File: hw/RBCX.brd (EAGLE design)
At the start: 100 x 100 mm, 463 parts, among them IC1 AMS1117-3.3, IC10 INA180A4, IC11 INA180A4, IC12 MPU-6050, IC13 STM32F103VCT6, IC2 DRV8833PWP, IC3 INA180A4, IC4 INA180A4, IC5 DRV8833PWP, IC6 INA180A4, IC7 INA180A4, IC8 INA180A4, IC9 INA180A4, P1 M1, P2 M2, P3 M3, P4 M4, Q1 NCE20P45Q, Q10 2N7002, Q2 NCE20P45Q, Q3 2N7002, Q4 2N7002, Q5 2N7002, Q6 2N7002, Q7 2N7002, Q8 2N7002, Q9 2N7002, X1 POWER_IN, X2 POWER_OUT, X3 52559-3092, X4 uUSB, Y1 5032/2P, Y2 3215_2P

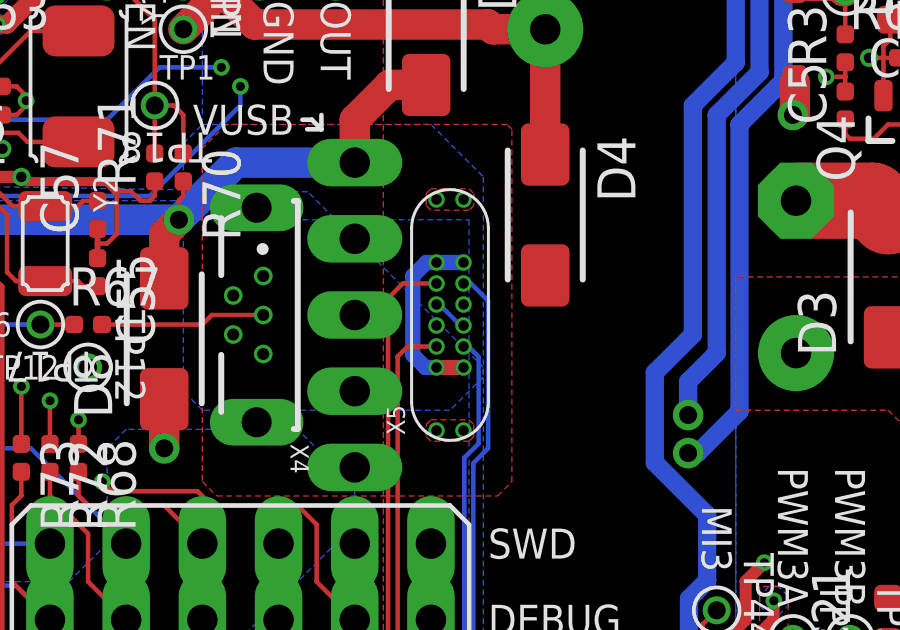
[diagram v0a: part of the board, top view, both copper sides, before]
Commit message: hw: change size of holes for USBC connector
- library `USB.lbr`
  - footprint `USB_C_8PIN` - change holes size from 0.35 mm to 0.30 mm to fit JLCPCB requirements
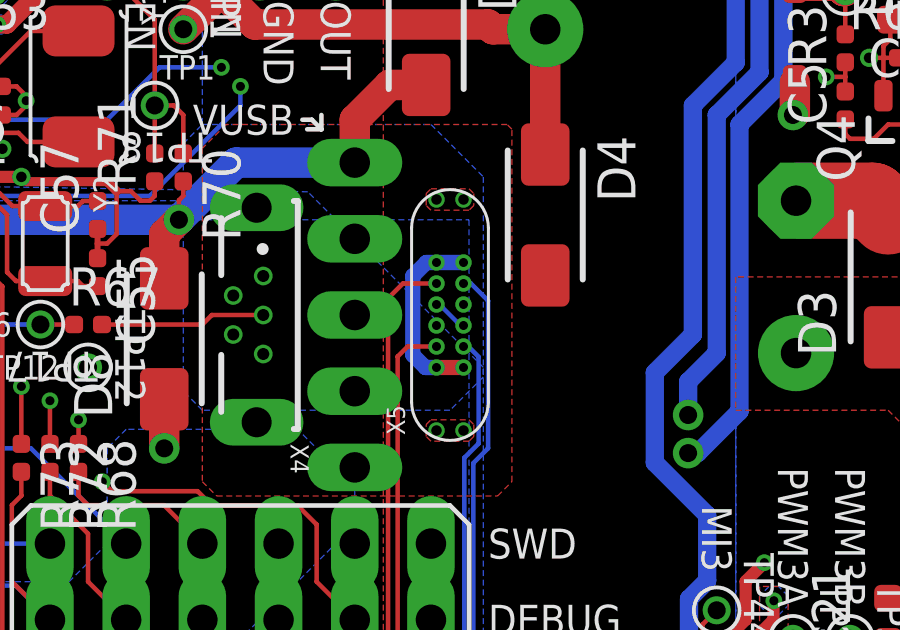
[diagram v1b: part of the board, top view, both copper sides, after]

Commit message: hw: change version to v1.2
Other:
- board text added: "Creative Commons Attribution-ShareAlike 4.0 License https://creativecommons.org/licenses/by-sa/4.0/ Designed by: Jaroslav Paral, Jakub Streit v1.2 9/2020 RB3204-RBCX https://github.com/RoboticsBrno/RB3204-RBCX"
- board text added: "RB3204-RBCX v1.2 9/2020 CC-SA 4.0 https://github.com/ RoboticsBrno/ RB3204-RBCX"
- board text removed: "Creative Commons Attribution-ShareAlike 4.0 License https://creativecommons.org/licenses/by-sa/4.0/ Designed by: Jaroslav Paral, Jakub Streit v1.1 6/2020 RB3204-RBCX https://github.com/RoboticsBrno/RB3204-RBCX"
- board text removed: "RB3204-RBCX v1.1 6/2020 CC-SA 4.0 https://github.com/ RoboticsBrno/ RB3204-RBCX"

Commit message: hw: change resistors R20 - R23 valu to 2k2 (VUSB and ESP_+5V power LED resistors)
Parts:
- R20, R21, R22, R23: value 1k -> 2k2
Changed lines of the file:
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@@
 <attribute name="VALUE" x="2.2225" y="67.78625" size="1.27" layer="28" rot="MR0"/>
 </element>
-<element name="R20" library="rcl_upravena" package="R0402" value="1k" x="93.345" y="88.9" smashed="yes">
+<element name="R20" library="rcl_upravena" package="R0402" value="2k2" x="93.345" y="88.9" smashed="yes">
 <attribute name="NAME" x="92.71" y="89.535" size="1.27" layer="25"/>
 <attribute name="VALUE" x="92.71" y="86.995" size="1.27" layer="27"/>
 </element>
-<element name="R22" library="rcl_upravena" package="R0402" value="1k" x="97.79" y="88.9" smashed="yes">
+<element name="R22" library="rcl_upravena" package="R0402" value="2k2" x="97.79" y="88.9" smashed="yes">
 <attribute name="NAME" x="97.155" y="89.535" size="1.27" layer="25"/>
 <attribute name="VALUE" x="97.155" y="86.995" size="1.27" layer="27"/>
@@
 <attribute name="VALUE" x="95.885" y="89.05875" size="1.27" layer="27" rot="R270"/>
 </element>
-<element name="R21" library="rcl_upravena" package="R0402" value="1k" x="93.345" y="88.9" smashed="yes" rot="MR180">
+<element name="R21" library="rcl_upravena" package="R0402" value="2k2" x="93.345" y="88.9" smashed="yes" rot="MR180">
 <attribute name="NAME" x="92.71" y="88.265" size="1.27" layer="26" rot="MR180"/>
 <attribute name="VALUE" x="92.71" y="90.805" size="1.27" layer="28" rot="MR180"/>
 </element>
-<element name="R23" library="rcl_upravena" package="R0402" value="1k" x="97.79" y="88.9" smashed="yes" rot="MR180">
+<element name="R23" library="rcl_upravena" package="R0402" value="2k2" x="97.79" y="88.9" smashed="yes" rot="MR180">
 <attribute name="NAME" x="97.155" y="88.265" size="1.27" layer="26" rot="MR180"/>
 <attribute name="VALUE" x="97.155" y="90.805" size="1.27" layer="28" rot="MR180"/>

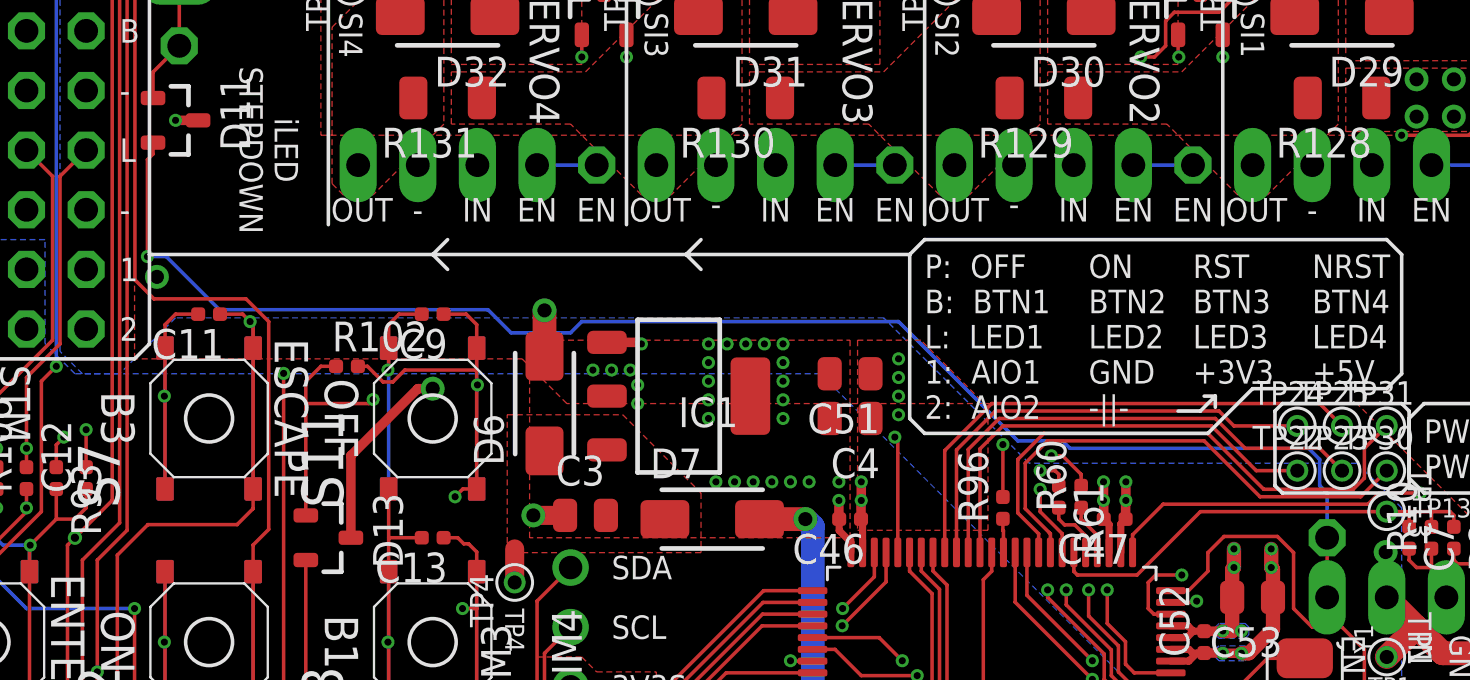
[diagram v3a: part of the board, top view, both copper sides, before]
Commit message: hw: disconnect 3V3_EN and D11 (this connection prevents main step-down IM1 from startup)
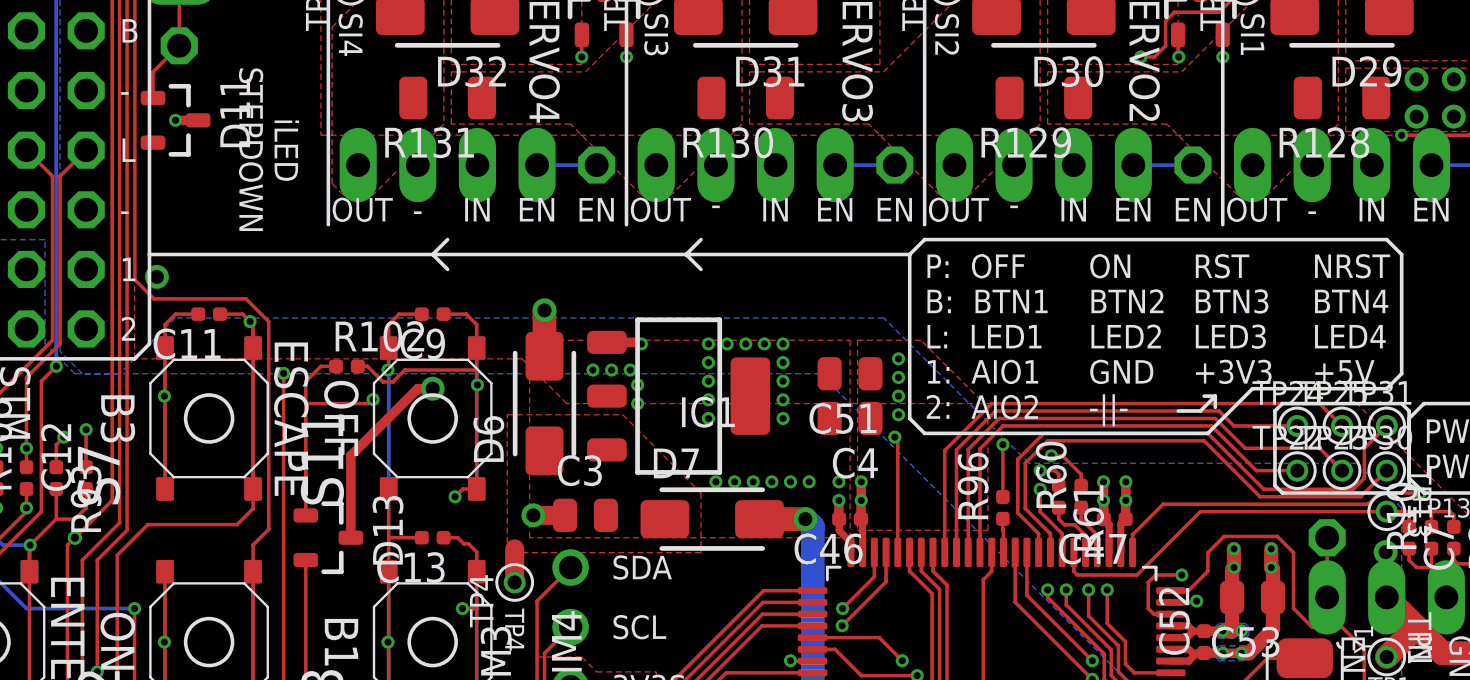
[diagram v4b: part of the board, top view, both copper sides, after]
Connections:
- new net D11_NC: D11.2
- net 3V3_EN: no longer D11.2
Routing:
- net 3V3_EN: track 64.9 -> 2.54 mm, vias 1 -> 0

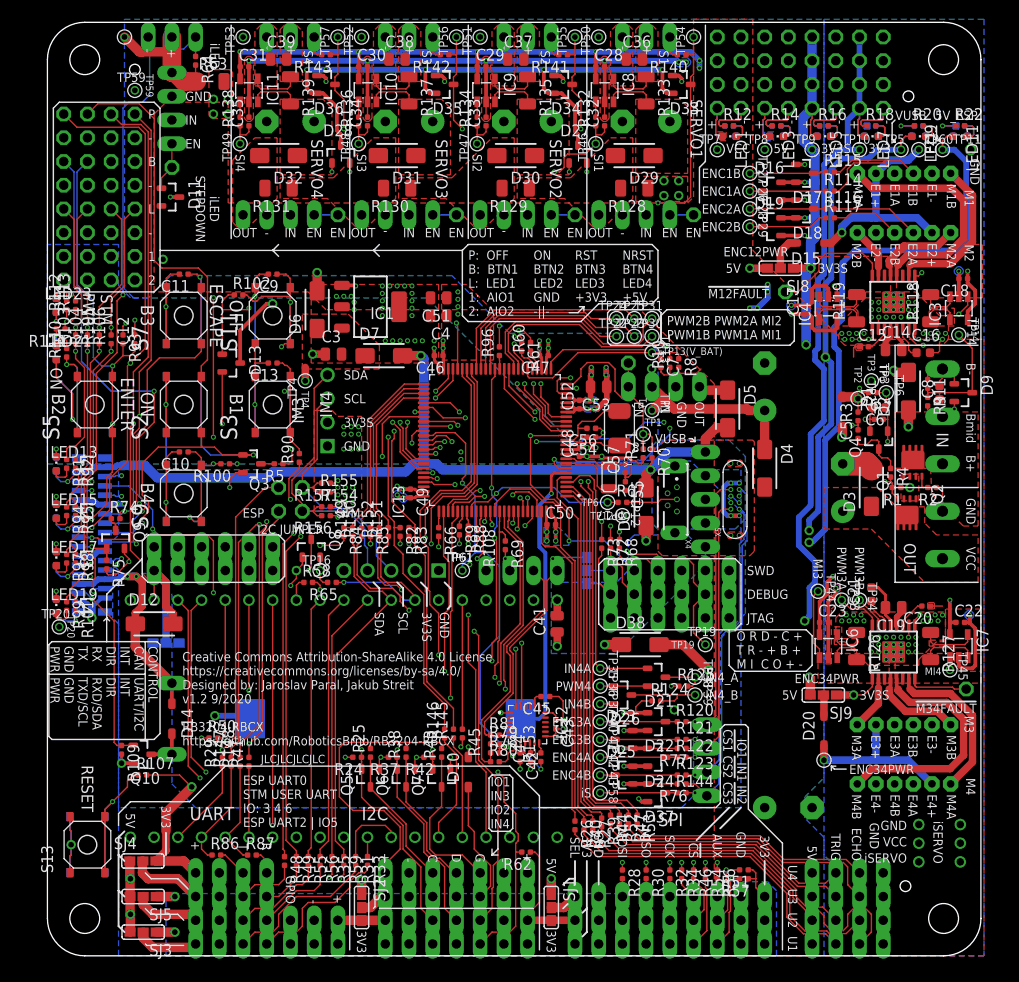
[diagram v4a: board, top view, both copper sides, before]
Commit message: hw: fix jst connectors drill (motor connectors) and pad size (iServo connectors), move bottom pinheads to left to make enough space for iServo connectors
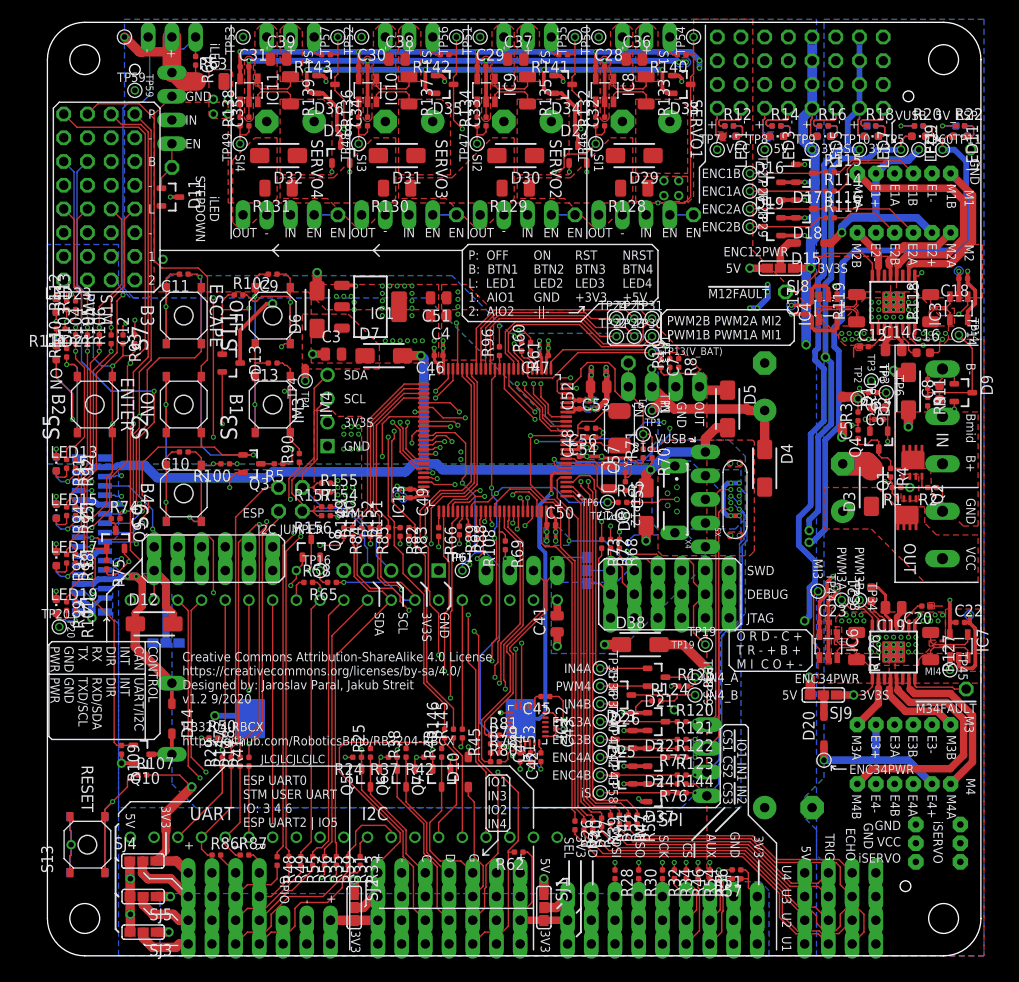
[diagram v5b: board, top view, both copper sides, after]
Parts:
- JP56, JP57: device iServo_connector:292161-3 -> jst-ph:JST-PH3
- moved JP10 0.79 mm to (48.1, 8.89)
- moved JP12 0.79 mm to (73.5, 6.35)
- moved JP14 0.79 mm to (39.2, 6.35)
- moved JP15 0.79 mm to (62.1, 3.81)
- moved JP17 0.79 mm to (48.1, 6.35)
- moved JP19 0.79 mm to (73.5, 3.81)
- moved JP21 0.79 mm to (62.1, 1.27)
- moved JP22 0.79 mm to (39.2, 3.81)
- moved JP24 0.79 mm to (73.5, 1.27)
- moved JP25 0.79 mm to (48.1, 3.81)
- moved JP28 0.79 mm to (39.2, 1.27)
- moved JP30 0.79 mm to (48.1, 1.27)
- moved JP7 0.79 mm to (39.2, 8.89)
- moved JP8 0.79 mm to (62.1, 6.35)
- moved R30 0.79 mm to (63.3, 8.73)
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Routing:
- net ESP-I2C-PWR: track 34.8 -> 33.2 mm
- net ESP-I2C-SCL: track 72.0 -> 70.8 mm
- net +3V3: track 122.0 -> 120.9 mm
- net GPIO-4: track 9.37 -> 8.44 mm
- net +3V3S: track 572.4 -> 571.6 mm
- net SPI_!SS3!/TDO: track 92.5 -> 91.7 mm
- net UTS2-ECHO: track 36.5 -> 35.7 mm
- net UTS1-TRIG: track 34.8 -> 34.0 mm
- net UTS3-ECHO: track 29.4 -> 28.6 mm
- net UTS4-TRIG: track 26.6 -> 25.8 mm
- net UTS4-ECHO: track 26.3 -> 25.5 mm
- net UTS1-ECHO: track 41.2 -> 40.4 mm
- net SPI_SCK: track 39.4 -> 38.6 mm
- net SPI_MOSI: track 52.1 -> 51.3 mm
- net SPI_MISO: track 39.4 -> 38.6 mm
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
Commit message: hw: move parts away from pins
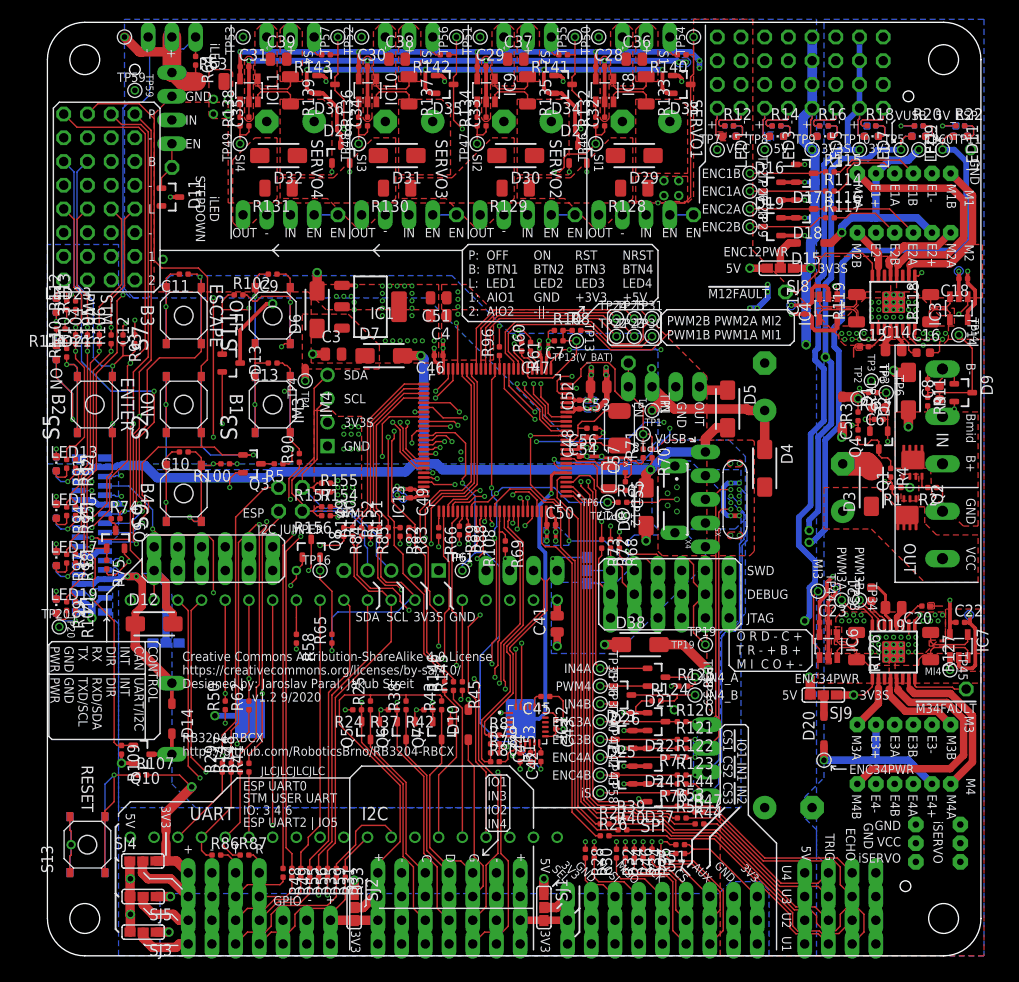
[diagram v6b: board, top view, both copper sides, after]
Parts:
- moved R62 32.9 mm to (21.6, 26.8), turned to 90 degrees
- moved R10 12.4 mm to (54.8, 67.0), turned to 0 degrees
- moved R8 11.5 mm to (56.7, 67.0), turned to 0 degrees
- moved C7 11.2 mm to (54.8, 65.9), turned to 180 degrees
- moved R44 9.54 mm to (69.8, 14.1), turned to 0 degrees
- moved TP13 8.20 mm to (56.7, 65.9)
- moved R54 8.09 mm to (61.9, 11.0)
- moved R47 7.66 mm to (69.8, 15.4), turned to 0 degrees
- moved R52 6.67 mm to (67.9, 14.8), turned to 0 degrees
- moved R51 6.61 mm to (67.8, 11.9)
- moved R57 6.61 mm to (67.8, 11.0)
- moved R36 6.58 mm to (64.8, 11.0)
- moved R58 6.16 mm to (26.7, 34.0), turned to 270 degrees
- moved R65 6.03 mm to (30.5, 34.0), turned to 90 degrees
- moved R46 5.98 mm to (62.9, 11.0)
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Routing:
- net UTS3-TRIG: track 26.8 -> 16.6 mm
- net ESP-I2C-SCL: track 70.8 -> 80.2 mm
- net UTS3_TRIG: track 38.1 -> 47.3 mm
- net VCC: track 82.0 -> 90.2 mm
- net V_BAT: track 20.0 -> 12.1 mm
- net UTS3-ECHO: track 28.6 -> 20.8 mm
- net SPI_!SS3!/TDO: track 91.7 -> 84.2 mm
- net UTS4-TRIG: track 25.8 -> 18.6 mm
- net UTS3_ECHO: track 60.4 -> 67.1 mm
- net GPIO1: track 73.4 -> 66.7 mm
- net ESP-SPI-!CS3: track 7.65 -> 14.2 mm
- net GPIO-1: track 1.92 -> 8.19 mm
- net UTS4_TRIG: track 39.3 -> 45.3 mm
- net ESP-SPI-MISO: track 7.00 -> 12.8 mm
- net ESP-SPI-SCK: track 7.00 -> 12.7 mm
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
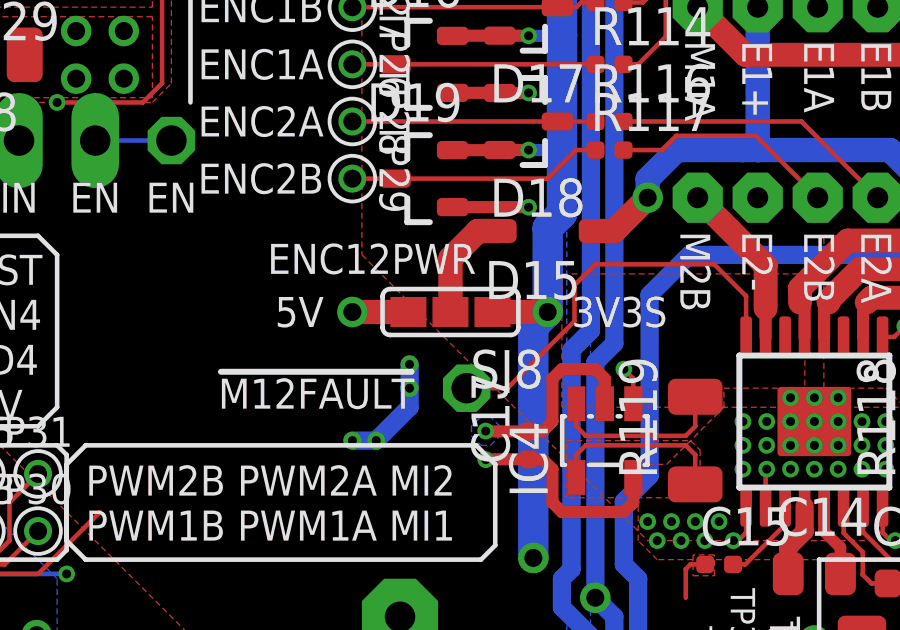
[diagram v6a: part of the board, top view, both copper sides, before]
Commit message: hw: add place for owner name
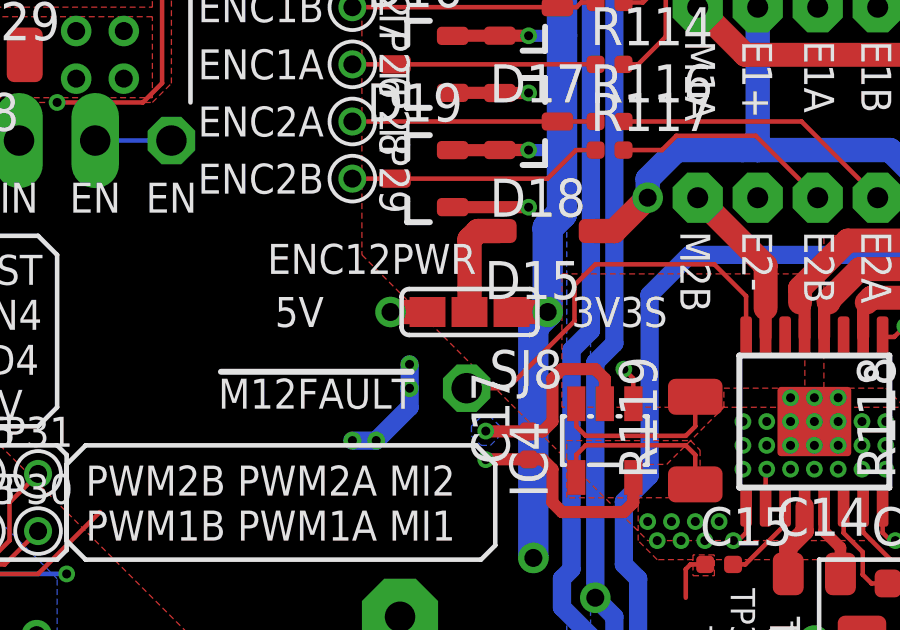
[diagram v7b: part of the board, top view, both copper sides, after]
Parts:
- moved SJ8 0.63 mm to (79.9, 73.7)
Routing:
- net GND: track 543.9 -> 544.6 mm
- net +5V: track 86.6 -> 86.0 mm
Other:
- board text added: "OWNER"
